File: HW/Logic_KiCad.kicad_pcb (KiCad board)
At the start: 4 copper layers, 100 x 100 mm, 248 parts, among them J1 USB_B_Micro, Q1 Q_NPN_BEC, Q2 Q_NPN_BEC, Q4 Q_NMOS_GSD, Q5 Q_PMOS_GSD, Q6 Q_NMOS_GSD, Q7 Q_PMOS_GSD, Q8 Q_NMOS_GSD, Q9 Q_PMOS_GSD, SW1 SW_SPDT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

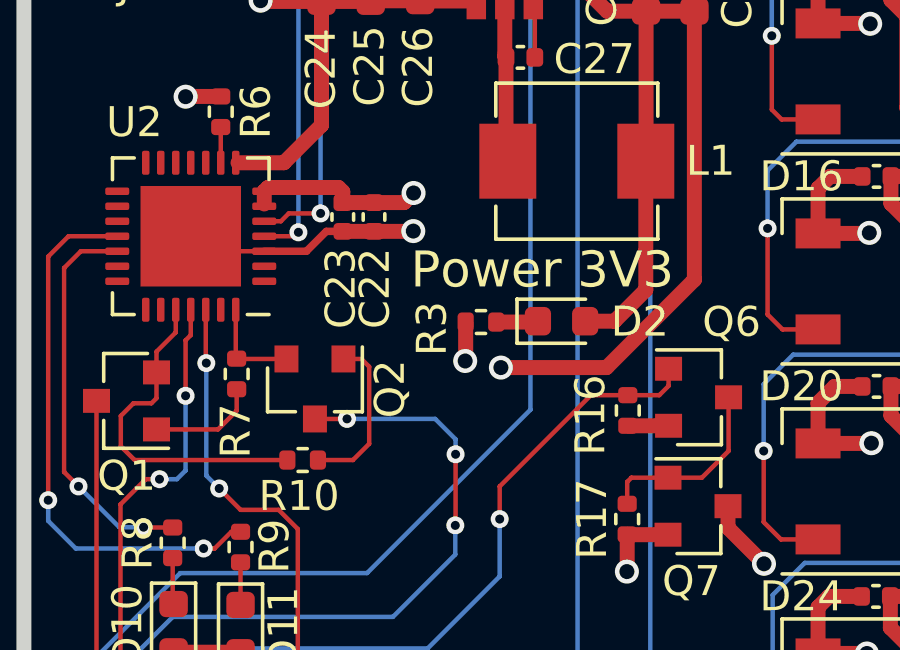
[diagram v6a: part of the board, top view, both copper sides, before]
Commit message: repair mistake in v1.0 - for fab, add to back-up v1.0 folder fab
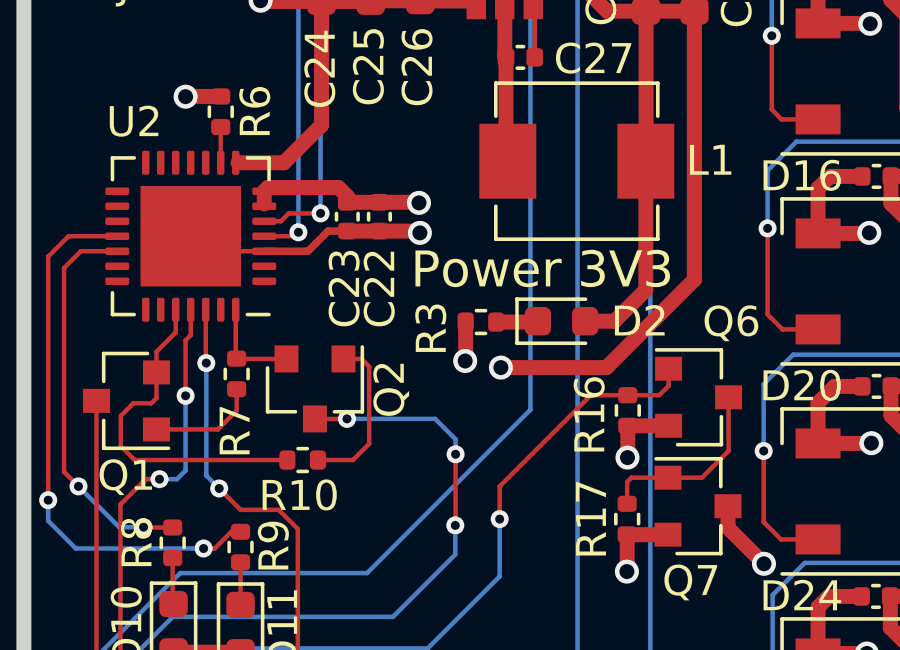
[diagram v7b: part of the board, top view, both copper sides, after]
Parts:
- moved C22 0.18 mm to (106.8, 66.4)
- moved C23 0.15 mm to (105.8, 66.4)
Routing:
- net GND: track 514.4 -> 515.7 mm, vias 122 -> 123
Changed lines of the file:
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@@
     (thickness 1.6)
     (drawings 23)
-    (tracks 2336)
+    (tracks 2339)
     (zones 0)
     (modules 248)
@@
   )
   (setup
-    (last_trace_width 0.15)
+    (last_trace_width 0.5)
     (user_trace_width 0.15)
     (user_trace_width 0.5)
@@
   )
   (module Capacitor_SMD:C_0402_1005Metric (layer F.Cu)
-    (at 106.67 66.4 90)
+    (at 106.85 66.39 90)
     (descr "Capacitor SMD 0402 (1005 Metric), square (rectangular) end terminal, IPC_7351 nominal, (Body size source: IPC-SM-782 page 76, https://www.pcb-3d.com/wordpress/wp-content/uploads/ipc-sm-782a_amendment_1_and_2.pdf), generated with kicad-footprint-generator")
     (tags capacitor)
@@
   )
   (module Capacitor_SMD:C_0402_1005Metric (layer F.Cu)
-    (at 105.63 66.4 90)
+    (at 105.78 66.39 90)
     (descr "Capacitor SMD 0402 (1005 Metric), square (rectangular) end terminal, IPC_7351 nominal, (Body size source: IPC-SM-782 page 76, https://www.pcb-3d.com/wordpress/wp-content/uploads/ipc-sm-782a_amendment_1_and_2.pdf), generated with kicad-footprint-generator")
     (tags capacitor)
@@
   (segment (start 108.05 46.556) (end 108.072 46.534) (width 0.5) (layer F.Cu) (net 2))
   (segment (start 108.05 48.62) (end 108.05 46.556) (width 0.5) (layer F.Cu) (net 2))
-  (segment (start 103.012 67.542) (end 104.418 67.542) (width 0.25) (layer F.Cu) (net 2))
-  (segment (start 105.08 66.88) (end 105.63 66.88) (width 0.25) (layer F.Cu) (net 2))
-  (segment (start 104.418 67.542) (end 105.08 66.88) (width 0.25) (layer F.Cu) (net 2))
-  (segment (start 105.63 66.88) (end 106.67 66.88) (width 0.5) (layer F.Cu) (net 2))
-  (via (at 107.98 66.87) (size 0.8) (drill 0.5) (layers F.Cu B.Cu) (net 2))
-  (segment (start 107.97 66.88) (end 107.98 66.87) (width 0.5) (layer F.Cu) (net 2))
-  (segment (start 106.67 66.88) (end 107.97 66.88) (width 0.5) (layer F.Cu) (net 2))
   (segment (start 116.49 73.36) (end 115.13 73.36) (width 0.5) (layer F.Cu) (net 2))
+  (segment (start 105.78 66.87) (end 106.85 66.87) (width 0.5) (layer F.Cu) (net 2))
+  (via (at 108.2 66.93) (size 0.8) (drill 0.5) (layers F.Cu B.Cu) (net 2))
+  (segment (start 108.14 66.87) (end 108.2 66.93) (width 0.5) (layer F.Cu) (net 2))
+  (segment (start 106.85 66.87) (end 108.14 66.87) (width 0.5) (layer F.Cu) (net 2))
+  (segment (start 105.14 66.87) (end 105.78 66.87) (width 0.25) (layer F.Cu) (net 2))
+  (segment (start 104.468 67.542) (end 105.14 66.87) (width 0.25) (layer F.Cu) (net 2))
+  (segment (start 103.012 67.542) (end 104.468 67.542) (width 0.25) (layer F.Cu) (net 2))
+  (via (at 115.12 74.42) (size 0.8) (drill 0.5) (layers F.Cu B.Cu) (net 2))
+  (segment (start 115.13 74.41) (end 115.12 74.42) (width 0.5) (layer F.Cu) (net 2))
+  (segment (start 115.13 73.36) (end 115.13 74.41) (width 0.5) (layer F.Cu) (net 2))
   (segment (start 113.79 55.09) (end 113.865 55.015) (width 0.5) (layer F.Cu) (net 3))
   (segment (start 112.94 55.09) (end 113.79 55.09) (width 0.5) (layer F.Cu) (net 3))
@@
   (segment (start 98.870999 92.640999) (end 98.84 92.61) (width 0.25) (layer F.Cu) (net 3))
   (segment (start 100.034977 92.640999) (end 98.870999 92.640999) (width 0.25) (layer F.Cu) (net 3))
-  (segment (start 106.67 65.92) (end 105.63 65.92) (width 0.5) (layer F.Cu) (net 3))
-  (segment (start 105.63 65.92) (end 105.63 65.56) (width 0.5) (layer F.Cu) (net 3))
   (segment (start 105.487 65.417) (end 103.137 65.417) (width 0.5) (layer F.Cu) (net 3))
-  (segment (start 105.63 65.56) (end 105.487 65.417) (width 0.5) (layer F.Cu) (net 3))
-  (via (at 107.99 65.6) (size 0.8) (drill 0.5) (layers F.Cu B.Cu) (net 3))
-  (segment (start 107.67 65.92) (end 107.99 65.6) (width 0.5) (layer F.Cu) (net 3))
-  (segment (start 106.67 65.92) (end 107.67 65.92) (width 0.5) (layer F.Cu) (net 3))
+  (segment (start 105.78 65.91) (end 106.85 65.91) (width 0.5) (layer F.Cu) (net 3))
+  (via (at 108.17 65.93) (size 0.8) (drill 0.5) (layers F.Cu B.Cu) (net 3))
+  (segment (start 108.15 65.91) (end 108.17 65.93) (width 0.5) (layer F.Cu) (net 3))
+  (segment (start 106.85 65.91) (end 108.15 65.91) (width 0.5) (layer F.Cu) (net 3))
+  (segment (start 105.78 65.71) (end 105.487 65.417) (width 0.5) (layer F.Cu) (net 3))
+  (segment (start 105.78 65.91) (end 105.78 65.71) (width 0.5) (layer F.Cu) (net 3))
   (segment (start 124.254 37.576) (end 124.254 38.584) (width 0.5) (layer F.Cu) (net 4))
   (segment (start 124.254 38.584) (end 124.82 39.15) (width 0.5) (layer F.Cu) (net 4))
@@
   (segment (start 107.43 52.41) (end 107.42 52.42) (width 0.15) (layer F.Cu) (net 28))
   (segment (start 107.43 49.14) (end 107.43 52.41) (width 0.15) (layer F.Cu) (net 28))
-  (segment (start 103.012 66.542) (end 103.568 66.542) (width 0.15) (layer F.Cu) (net 28))
   (via (at 104.89 66.28) (size 0.6) (drill 0.3) (layers F.Cu B.Cu) (net 28))
-  (segment (start 103.83 66.28) (end 104.89 66.28) (width 0.15) (layer F.Cu) (net 28))
-  (segment (start 103.568 66.542) (end 103.83 66.28) (width 0.15) (layer F.Cu) (net 28))
-  (segment (start 104.89 66.28) (end 104.89 56.78) (width 0.15) (layer B.Cu) (net 28))
+  (segment (start 103.012 66.542) (end 103.568 66.542) (width 0.15) (layer F.Cu) (net 28))
   (segment (start 107.42 54.25) (end 107.42 52.42) (width 0.15) (layer B.Cu) (net 28))
+  (segment (start 103.568 66.542) (end 103.83 66.28) (width 0.15) (layer F.Cu) (net 28))
+  (segment (start 103.83 66.28) (end 104.89 66.28) (width 0.15) (layer F.Cu) (net 28))
   (segment (start 104.89 56.78) (end 107.42 54.25) (width 0.15) (layer B.Cu) (net 28))
+  (segment (start 104.89 66.28) (end 104.89 56.78) (width 0.15) (layer B.Cu) (net 28))
   (segment (start 101.19 52.82) (end 103.05 52.82) (width 0.15) (layer F.Cu) (net 29))
   (segment (start 105.19 50.68) (end 105.95 50.68) (width 0.15) (layer F.Cu) (net 29))
@@
   (via (at 106.620282 52.398675) (size 0.6) (drill 0.3) (layers F.Cu B.Cu) (net 29))
   (segment (start 106.49 50.68) (end 106.620282 50.810282) (width 0.15) (layer F.Cu) (net 29))
-  (via (at 104.150002 66.91) (size 0.6) (drill 0.3) (layers F.Cu B.Cu) (net 29))
-  (segment (start 104.018002 67.042) (end 104.150002 66.91) (width 0.15) (layer F.Cu) (net 29))
-  (segment (start 103.012 67.042) (end 104.018002 67.042) (width 0.15) (layer F.Cu) (net 29))
-  (segment (start 104.150002 66.91) (end 104.150002 56.559998) (width 0.15) (layer B.Cu) (net 29))
   (segment (start 104.150002 56.559998) (end 106.620282 54.089718) (width 0.15) (layer B.Cu) (net 29))
+  (segment (start 104.150002 66.91) (end 104.150002 56.559998) (width 0.15) (layer B.Cu) (net 29))
   (segment (start 106.620282 54.089718) (end 106.620282 52.398675) (width 0.15) (layer B.Cu) (net 29))
+  (segment (start 104.018002 67.042) (end 104.150002 66.91) (width 0.15) (layer F.Cu) (net 29))
+  (via (at 104.150002 66.91) (size 0.6) (drill 0.3) (layers F.Cu B.Cu) (net 29))
+  (segment (start 103.012 67.042) (end 104.018002 67.042) (width 0.15) (layer F.Cu) (net 29))
   (segment (start 105.972 46.534) (end 104.626 46.534) (width 0.5) (layer F.Cu) (net 30))
   (segment (start 104.626 46.534) (end 103.02 48.14) (width 0.5) (layer F.Cu) (net 30))
